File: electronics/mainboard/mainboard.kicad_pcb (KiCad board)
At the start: 2 copper layers, 55.5 x 56 mm, 11 parts, among them J1 USB_C_Receptacle_USB2.0_14P, SW1 SW_SPST, SW2 SW_SPST, SW3 SW_SPST, SW4 SW_SPST, SW5 SW_SPST, SW6 SW_SPST, SW7 SW_SPST, SW8 SW_SPST, SW9 SW_SPST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

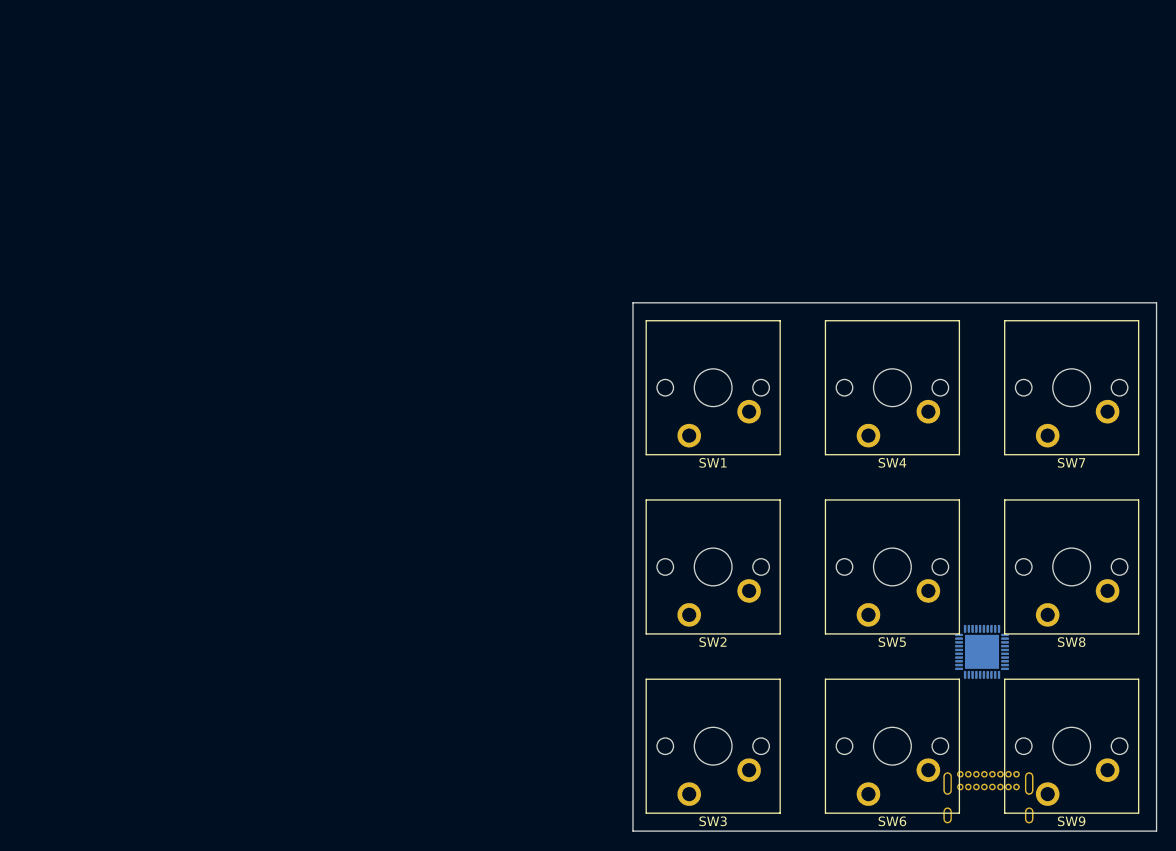
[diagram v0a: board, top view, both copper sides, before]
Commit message: Add gitattributes. Layout position of switches and board outline
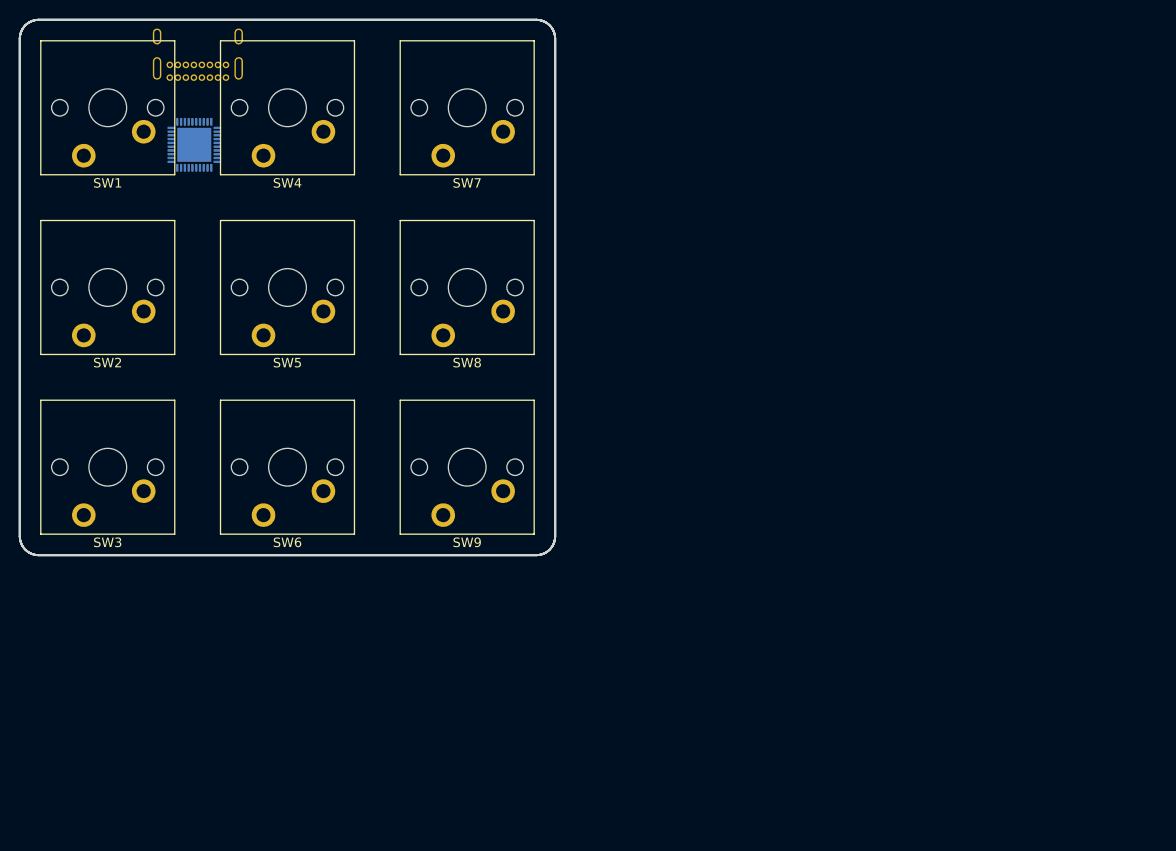
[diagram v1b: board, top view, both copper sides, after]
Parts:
- moved J1 116.2 mm to (56.9, 35.6), turned to 0 degrees
- moved U1 99.3 mm to (59.5, 42.8), turned to 0 degrees
- moved SW1 70.7 mm to (50.3, 38.8)
- moved SW2 70.7 mm to (50.3, 57.9)
- moved SW3 70.7 mm to (50.3, 76.9)
- moved SW4 70.7 mm to (69.4, 38.8)
- moved SW5 70.6 mm to (69.4, 57.9)
- moved SW6 70.6 mm to (69.4, 76.9)
- moved SW7 70.6 mm to (88.4, 38.8)
- moved SW8 70.6 mm to (88.4, 57.9)
- moved SW9 70.6 mm to (88.4, 76.9)
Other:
- board size 55.5 x 56 mm -> 56.8 x 56.8 mm

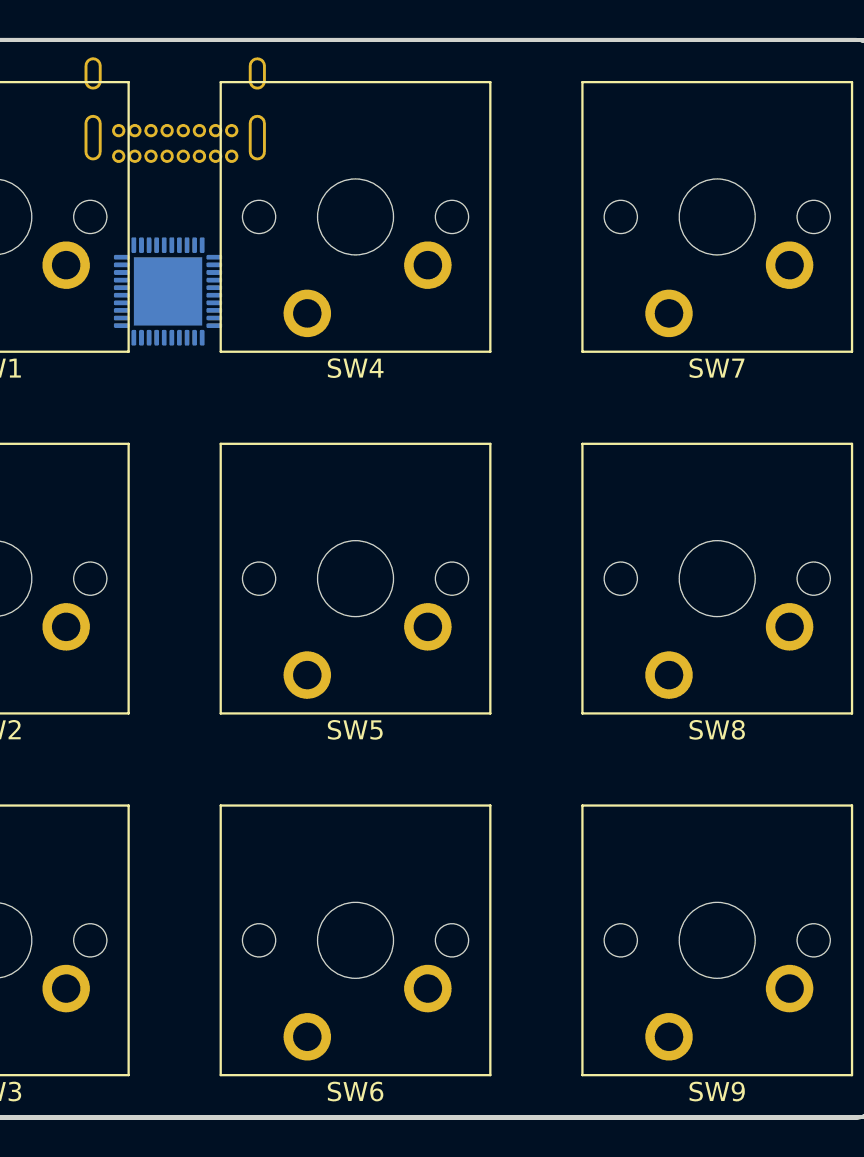
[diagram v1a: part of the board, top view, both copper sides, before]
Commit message: Add system diagram. Add project symbol library. Add fundamental components to schematic.
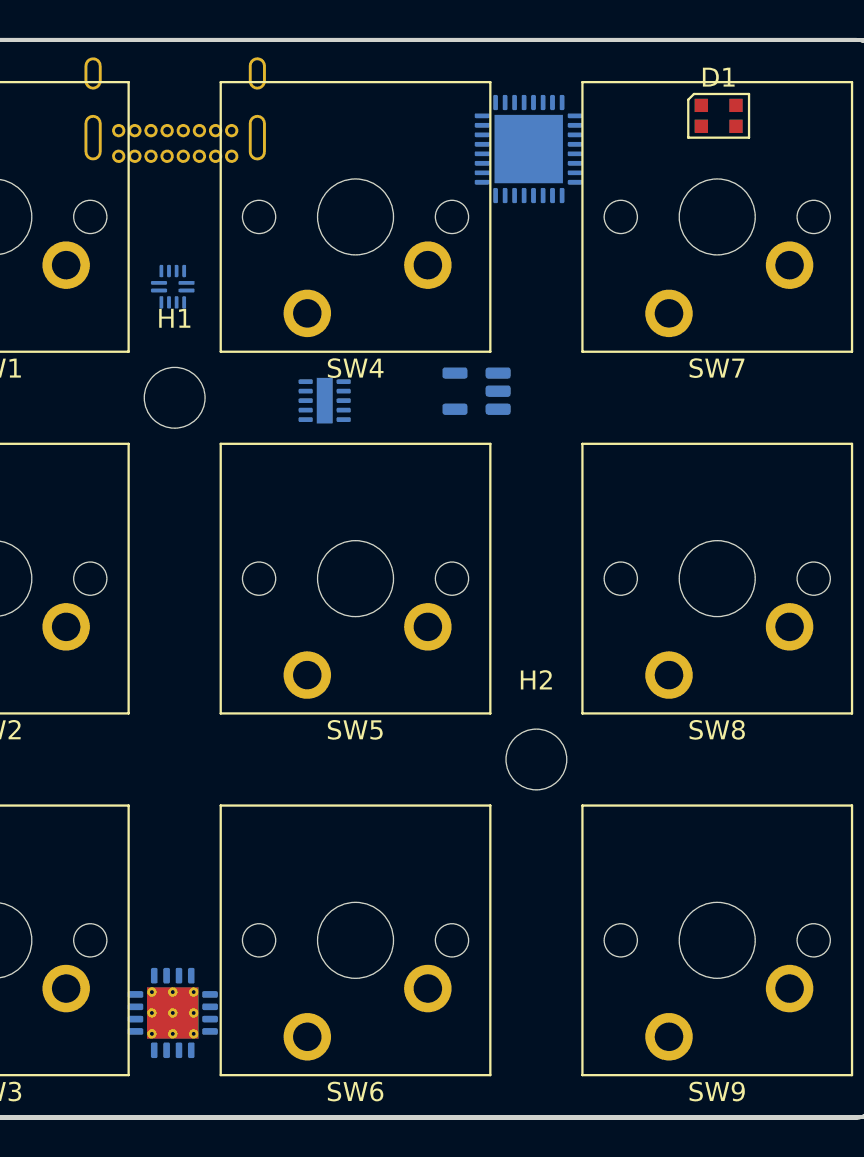
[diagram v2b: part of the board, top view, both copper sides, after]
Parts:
- added D1: WS2812B-2020, LED_SMD:LED_WS2812B-2020_PLCC4_2.0x2.0mm, F.Cu at (88.5, 33.5)
- added H1: MountingHole_Pad, MountingHole:MountingHole_3.2mm_M3, F.Cu at (59.9, 48.4)
- added H2: MountingHole_Pad, MountingHole:MountingHole_3.2mm_M3, F.Cu at (78.9, 67.4)
- added U2: STLQ020C33R, Package_TO_SOT_SMD:SOT-23-5, B.Cu at (75.8, 48.0)
- added U3: FUSB303BTMX, Package_DFN_QFN:Texas_X2QFN-12_1.6x1.6mm_P0.4mm, B.Cu at (59.8, 42.5)
- added U4: BQ25060DQCR, Package_SON:WSON-10-1EP_2x3mm_P0.5mm_EP0.84x2.4mm, B.Cu at (67.8, 48.5)
- added U5: TPS61092, Package_DFN_QFN:Texas_RSA_VQFN-16-1EP_4x4mm_P0.65mm_EP2.7x2.7mm_ThermalVias, B.Cu at (59.8, 80.8)
- U1: value ESP32-C6 -> ESP32-C6FH4; footprint Package_DFN_QFN:QFN-40-1EP_5x5mm_P0.4mm_EP3.6x3.6mm -> Package_DFN_QFN:QFN-32-1EP_5x5mm_P0.5mm_EP3.6x3.6mm
- moved U1 20.4 mm to (78.5, 35.2), turned to 180 degrees
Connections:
- J1 pad A6: Net-(U1-GPIO13/USB_D+) -> Net-(J1-D+-PadA6)
- J1 pad A7: Net-(U1-GPIO12/USB_D-) -> Net-(J1-D--PadA7)
- J1 pad B6: Net-(U1-GPIO13/USB_D+) -> Net-(J1-D+-PadA6)
- J1 pad B7: Net-(U1-GPIO12/USB_D-) -> Net-(J1-D--PadA7)
- U1 pad 18: Net-(U1-GPIO12/USB_D-) -> unconnected-(U1-GPIO14-Pad18)
- U1 pad 19: Net-(U1-GPIO13/USB_D+) -> unconnected-(U1-GPIO15-Pad19)
